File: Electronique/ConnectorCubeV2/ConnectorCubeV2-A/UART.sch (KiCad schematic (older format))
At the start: 18 parts, among them J901 Conn_01x04, J902 Conn_01x04, J903 Conn_01x04, Q901 BSS123, Q902 BSS123, Q903 BSS123

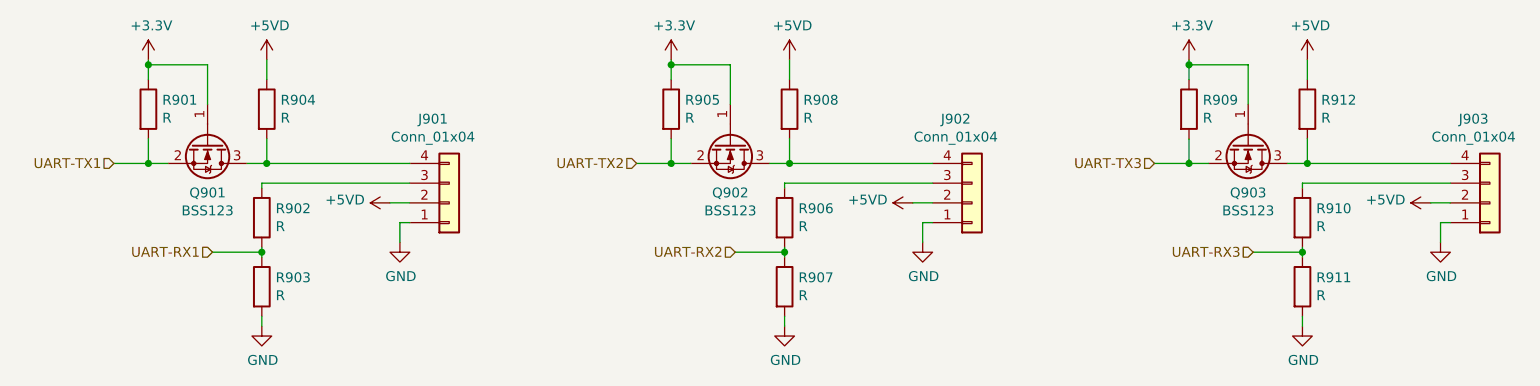
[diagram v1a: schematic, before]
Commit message: V206 TM1638 7Segments Begin
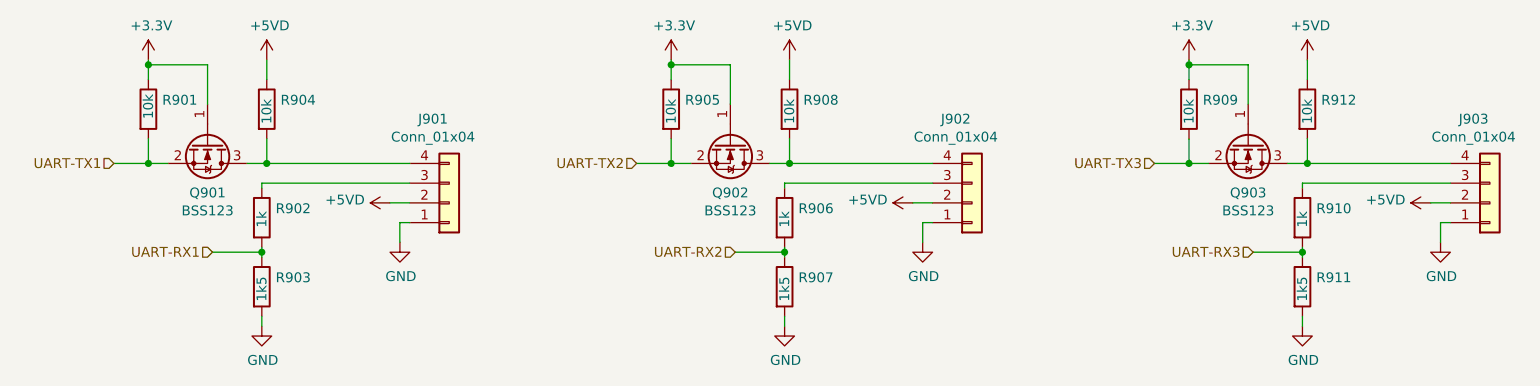
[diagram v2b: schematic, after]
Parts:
- R901, R904, R905, R908, R909, R912: value R -> 10k
- R902, R906, R910: value R -> 1k
- R903, R907, R911: value R -> 1k5
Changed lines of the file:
@@
 P 3300 4300
 F 0 "R903" H 3370 4346 50  0000 L CNN
-F 1 "R" H 3370 4255 50  0000 L CNN
+F 1 "1k5" V 3300 4225 50  0000 L CNN
 F 2 "Resistor_SMD:R_0603_1608Metric" V 3230 4300 50  0001 C CNN
 F 3 "~" H 3300 4300 50  0001 C CNN
@@
 P 3300 3950
 F 0 "R902" H 3370 3996 50  0000 L CNN
-F 1 "R" H 3370 3905 50  0000 L CNN
+F 1 "1k" V 3300 3900 50  0000 L CNN
 F 2 "Resistor_SMD:R_0603_1608Metric" V 3230 3950 50  0001 C CNN
 F 3 "~" H 3300 3950 50  0001 C CNN
@@
 P 2725 3400
 F 0 "R901" H 2795 3446 50  0000 L CNN
-F 1 "R" H 2795 3355 50  0000 L CNN
+F 1 "10k" V 2725 3350 50  0000 L CNN
 F 2 "Resistor_SMD:R_0603_1608Metric" V 2655 3400 50  0001 C CNN
 F 3 "~" H 2725 3400 50  0001 C CNN
@@
 P 3325 3400
 F 0 "R904" H 3395 3446 50  0000 L CNN
-F 1 "R" H 3395 3355 50  0000 L CNN
+F 1 "10k" V 3325 3325 50  0000 L CNN
 F 2 "Resistor_SMD:R_0603_1608Metric" V 3255 3400 50  0001 C CNN
 F 3 "~" H 3325 3400 50  0001 C CNN
@@
 P 5950 4300
 F 0 "R907" H 6020 4346 50  0000 L CNN
-F 1 "R" H 6020 4255 50  0000 L CNN
+F 1 "1k5" V 5950 4225 50  0000 L CNN
 F 2 "Resistor_SMD:R_0603_1608Metric" V 5880 4300 50  0001 C CNN
 F 3 "~" H 5950 4300 50  0001 C CNN
@@
 P 5950 3950
 F 0 "R906" H 6020 3996 50  0000 L CNN
-F 1 "R" H 6020 3905 50  0000 L CNN
+F 1 "1k" V 5950 3900 50  0000 L CNN
 F 2 "Resistor_SMD:R_0603_1608Metric" V 5880 3950 50  0001 C CNN
 F 3 "~" H 5950 3950 50  0001 C CNN
@@
 P 5375 3400
 F 0 "R905" H 5445 3446 50  0000 L CNN
-F 1 "R" H 5445 3355 50  0000 L CNN
+F 1 "10k" V 5375 3325 50  0000 L CNN
 F 2 "Resistor_SMD:R_0603_1608Metric" V 5305 3400 50  0001 C CNN
 F 3 "~" H 5375 3400 50  0001 C CNN
@@
 P 5975 3400
 F 0 "R908" H 6045 3446 50  0000 L CNN
-F 1 "R" H 6045 3355 50  0000 L CNN
+F 1 "10k" V 5975 3325 50  0000 L CNN
 F 2 "Resistor_SMD:R_0603_1608Metric" V 5905 3400 50  0001 C CNN
 F 3 "~" H 5975 3400 50  0001 C CNN
@@
 P 8575 4300
 F 0 "R911" H 8645 4346 50  0000 L CNN
-F 1 "R" H 8645 4255 50  0000 L CNN
+F 1 "1k5" V 8575 4225 50  0000 L CNN
 F 2 "Resistor_SMD:R_0603_1608Metric" V 8505 4300 50  0001 C CNN
 F 3 "~" H 8575 4300 50  0001 C CNN
@@
 P 8575 3950
 F 0 "R910" H 8645 3996 50  0000 L CNN
-F 1 "R" H 8645 3905 50  0000 L CNN
+F 1 "1k" V 8575 3900 50  0000 L CNN
 F 2 "Resistor_SMD:R_0603_1608Metric" V 8505 3950 50  0001 C CNN
 F 3 "~" H 8575 3950 50  0001 C CNN
@@
 P 8000 3400
 F 0 "R909" H 8070 3446 50  0000 L CNN
-F 1 "R" H 8070 3355 50  0000 L CNN
+F 1 "10k" V 8000 3325 50  0000 L CNN
 F 2 "Resistor_SMD:R_0603_1608Metric" V 7930 3400 50  0001 C CNN
 F 3 "~" H 8000 3400 50  0001 C CNN
@@
 P 8600 3400
 F 0 "R912" H 8670 3446 50  0000 L CNN
-F 1 "R" H 8670 3355 50  0000 L CNN
+F 1 "10k" V 8600 3325 50  0000 L CNN
 F 2 "Resistor_SMD:R_0603_1608Metric" V 8530 3400 50  0001 C CNN
 F 3 "~" H 8600 3400 50  0001 C CNN
